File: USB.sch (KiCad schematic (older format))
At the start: 49 parts

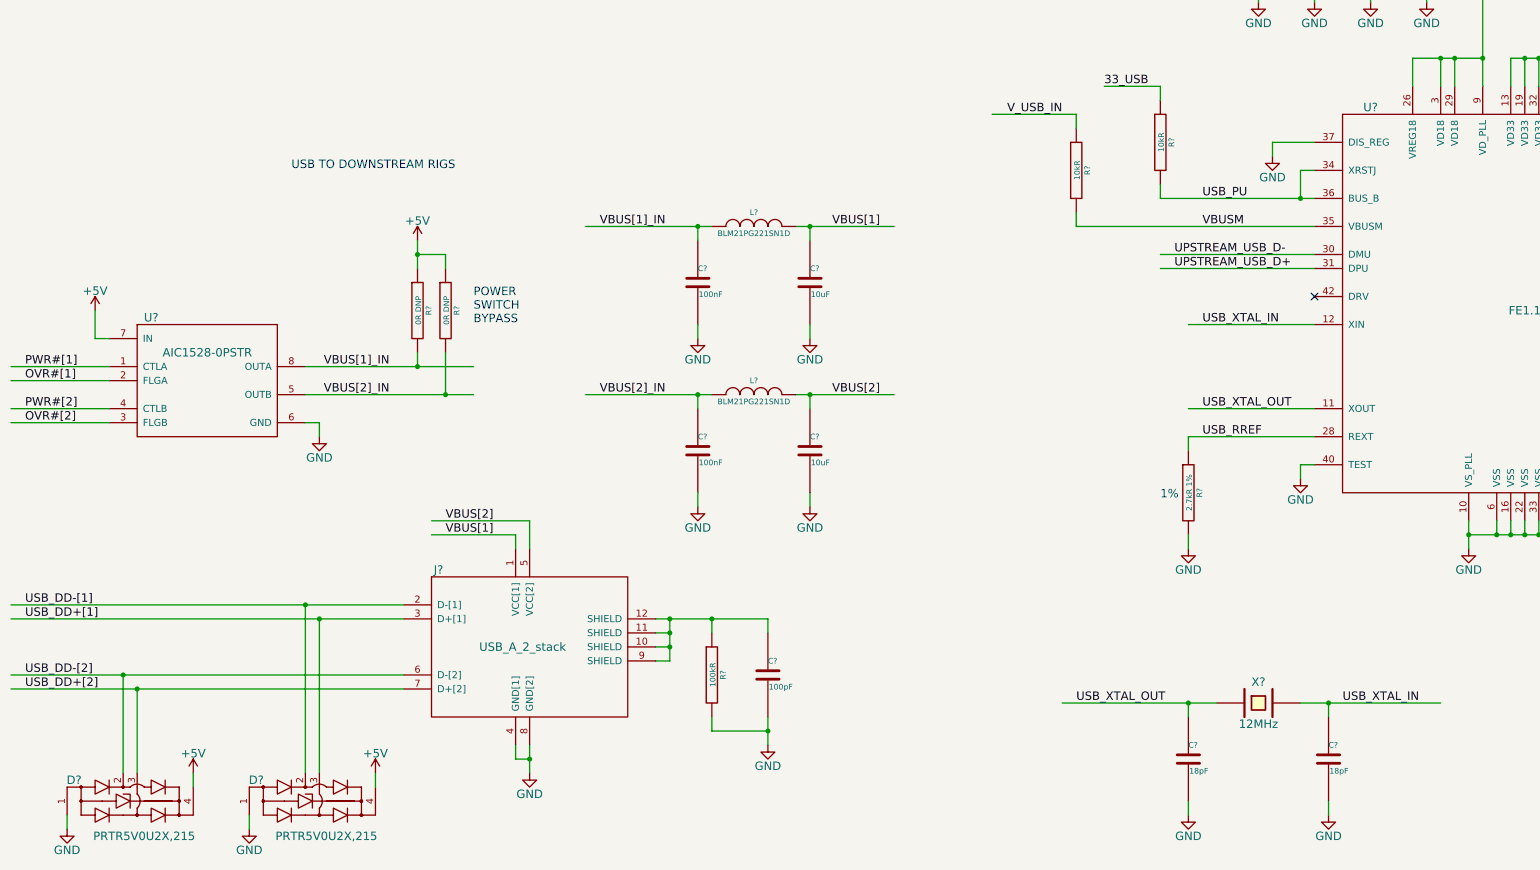
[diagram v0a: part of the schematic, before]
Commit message: added testpoint part number, small net naming changes
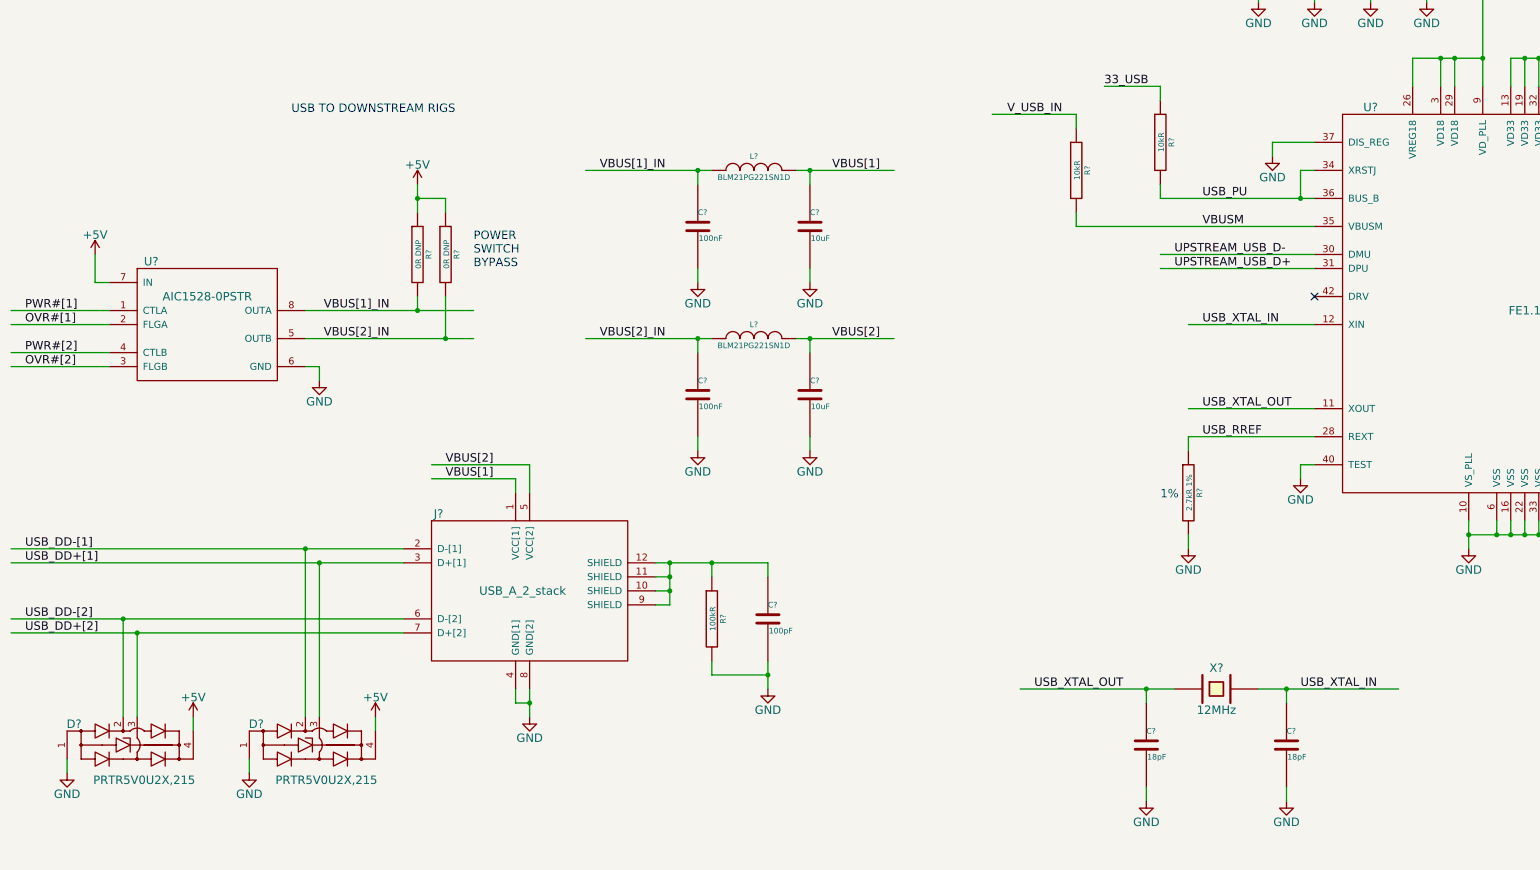
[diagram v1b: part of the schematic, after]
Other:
- moved on the sheet: C?, D?, J?, L?, R?, U?, X?

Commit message: annotated
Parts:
- gave numbers to parts that had none: 49

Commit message: annotated, netlist
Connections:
- wire segments 261 -> 199

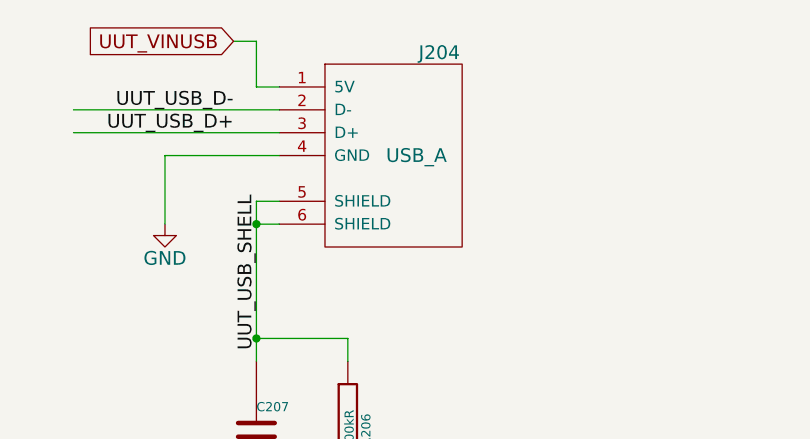
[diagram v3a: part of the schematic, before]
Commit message: swapped out new USB_A_TH symbol
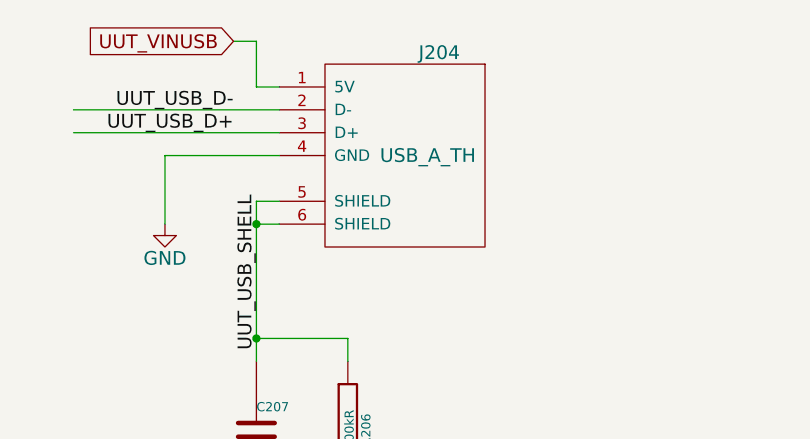
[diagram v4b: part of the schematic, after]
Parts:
- removed J204: USB_A, symbol USB_A
- added J204: USB_A_TH, symbol USB_A_TH
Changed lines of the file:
@@
 EESchema Schematic File Version 2
+LIBS:t2-hw-test-rig-rescue
 LIBS:power
 LIBS:device
@@
 LIBS:memory
 LIBS:xilinx
-LIBS:special
 LIBS:microcontrollers
 LIBS:dsp
@@
 	3650 3100 3650 3200
 $Comp
-L USB_A J204
-U 1 1 55427432
-P 9000 2000
-F 0 "J204" H 8900 2450 60  0000 C CNN
-F 1 "USB_A" H 9000 2000 60  0000 C CNN
-F 2 "" H 9600 2500 60  0000 C CNN
-F 3 "" H 9600 2500 60  0000 C CNN
-	1    9000 2000
-	-1   0    0    -1
-$EndComp
-$Comp
 L GND #PWR054
 U 1 1 554278A0
@@
 Wire Wire Line
 	8300 1500 8200 1500
+$Comp
+L USB_A_TH J204
+U 1 1 5547C2A7
+P 9000 2000
+F 0 "J204" H 8900 2450 60  0000 C CNN
+F 1 "USB_A_TH" H 8950 2000 60  0000 C CNN
+F 2 "" H 9600 2500 60  0000 C CNN
+F 3 "" H 9600 2500 60  0000 C CNN
+	1    9000 2000
+	-1   0    0    -1
+$EndComp
 $EndSCHEMATC

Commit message: unconventional library hack:moved tm lib above all others so parts come from there first
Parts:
- J204: footprint (none) -> tm-kicad-lib:USB-A
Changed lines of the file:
@@
 EESchema Schematic File Version 2
-LIBS:t2-hw-test-rig-rescue
+LIBS:tm-kicad-lib
 LIBS:power
 LIBS:device
@@
 LIBS:contrib
 LIBS:valves
-LIBS:tm-kicad-lib
 LIBS:t2-hw-test-rig-cache
 EELAYER 25 0
@@
 F 0 "J204" H 8900 2450 60  0000 C CNN
 F 1 "USB_A_TH" H 8950 2000 60  0000 C CNN
-F 2 "" H 9600 2500 60  0000 C CNN
+F 2 "tm-kicad-lib:USB-A" H 9600 2500 60  0001 C CNN
 F 3 "" H 9600 2500 60  0000 C CNN
 	1    9000 2000

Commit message: components and footprints
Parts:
- C222, C223: footprint tm-kicad-lib:SMD-0402-C -> tm-kicad-lib:SMD-0402
- J202: footprint (none) -> Pin_Headers:Pin_Header_Straight_1x02
- R203, R204: footprint tm-kicad-lib:SMD-0603-R -> tm-kicad-lib:SMD-0603
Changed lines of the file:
@@
 F 0 "R203" V 4280 6000 40  0000 C CNN
 F 1 "0R DNP" V 4207 6001 40  0000 C CNN
-F 2 "tm-kicad-lib:SMD-0603-R" V 4130 6000 30  0001 C CNN
+F 2 "tm-kicad-lib:SMD-0603" V 4130 6000 30  0001 C CNN
 F 3 "" H 4200 6000 30  0000 C CNN
 	1    4200 6000
@@
 	2200 3100 2200 3000
 Wire Wire Line
-	1800 3000 2200 3000
+	2200 3000 1800 3000
 Wire Wire Line
 	1800 2200 1800 3100
@@
 F 0 "R204" V 4480 6000 40  0000 C CNN
 F 1 "0R DNP" V 4407 6001 40  0000 C CNN
-F 2 "tm-kicad-lib:SMD-0603-R" V 4330 6000 30  0001 C CNN
+F 2 "tm-kicad-lib:SMD-0603" V 4330 6000 30  0001 C CNN
 F 3 "" H 4400 6000 30  0000 C CNN
 	1    4400 6000
@@
 F 0 "C223" H 16100 7500 40  0000 L CNN
 F 1 "1uF DNP" H 16106 7315 40  0000 L CNN
-F 2 "tm-kicad-lib:SMD-0402-C" H 16138 7250 30  0001 C CNN
+F 2 "tm-kicad-lib:SMD-0402" H 16138 7250 30  0001 C CNN
 F 3 "" H 16100 7400 60  0000 C CNN
 	1    16100 7400
@@
 F 0 "C222" H 15700 7500 40  0000 L CNN
 F 1 "1uF DNP" H 15706 7315 40  0000 L CNN
-F 2 "tm-kicad-lib:SMD-0402-C" H 15738 7250 30  0001 C CNN
+F 2 "tm-kicad-lib:SMD-0402" H 15738 7250 30  0001 C CNN
 F 3 "" H 15700 7400 60  0000 C CNN
 	1    15700 7400
@@
 F 0 "J202" H 4850 2050 50  0000 C CNN
 F 1 "CONN_01X02" V 4950 1900 50  0000 C CNN
-F 2 "" H 4850 1900 60  0000 C CNN
+F 2 "Pin_Headers:Pin_Header_Straight_1x02" H 4850 1900 60  0001 C CNN
 F 3 "" H 4850 1900 60  0000 C CNN
 	1    4850 1900
@@
 F 0 "JP201" H 4700 1750 50  0000 C CNN
 F 1 "JUMPER" H 4700 1520 50  0000 C CNN
-F 2 "" H 4700 1600 60  0000 C CNN
+F 2 "" H 4700 1600 60  0001 C CNN
 F 3 "" H 4700 1600 60  0000 C CNN
 	1    4700 1600
@@
 	8700 2900 8700 2800
 Wire Wire Line
-	8300 2800 8700 2800
+	8700 2800 8300 2800
 Wire Wire Line
 	8300 2200 8300 2900

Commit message: usb refactor on sch and pcb, mechanical constraints on bcp
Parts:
- removed C203, C209, C211, C212, C214, C215, C217: 100nF, tm-kicad-lib:SMD-0402-C, symbol TM_C
- removed C204: 100pF, tm-kicad-lib:SMD-0402-C, symbol TM_C
- removed C205, C206, C213, C216, C218, C219: 10uF, tm-kicad-lib:SMD-0805-C, symbol TM_C
- removed C208, C210: 18pF, tm-kicad-lib:SMD-0402-C, symbol TM_C
- removed C220, C221: 1uF, tm-kicad-lib:SMD-0402-C, symbol TM_C
- removed C222, C223: 1uF DNP, tm-kicad-lib:SMD-0402, symbol TM_C
- removed D202: PRTR5V0U2X,215, tm-kicad-lib:PRTR5V0U2X,215, symbol PRTR5V0U2X,215
- removed J203: USB_A_2_stack, tm-kicad-lib:Molex-0672983090, symbol USB_A_2_stack
- removed L201, L202: BLM21PG221SN1D, tm-kicad-lib:SMD-0805-R, symbol TM_L
- removed R204: 0R DNP, tm-kicad-lib:SMD-0603, symbol TM_R
- removed R205: 100kR, tm-kicad-lib:SMD-0402-R, symbol TM_R
- removed R207, R208: 10kR, tm-kicad-lib:SMD-0402-R, symbol TM_R
- removed R209: 2.7kR 1%, tm-kicad-lib:SMD-0402-R, symbol TM_R
- removed R210, R211, R212, R213: 1MR, tm-kicad-lib:SMD-0402-R, symbol TM_R
- removed U201: AIC1528-0PSTR, tm-kicad-lib:SOP-8, symbol AIC1528-0PSTR
- removed U202: FE1.1, tm-kicad-lib:CY7C65634-48AXCT, symbol FE1.1
- removed X201: 12MHz, tm-kicad-lib:Seeed-xtal-12MHz, symbol CRYSTAL
- added J203: MICROUSB-TH, tm-kicad-lib:Seeed-USB-Micro-320010028, symbol MICROUSB-TH
- C202: value 100nF -> 100pF
- R203: value 0R DNP -> 100kR; footprint tm-kicad-lib:SMD-0603 -> tm-kicad-lib:SMD-0402-R
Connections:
- net labels added: UUT_USB_PASSTHROUGH_SHELL
- net labels removed: 33_USB, OVR#[1], OVR#[2], PWR#[1], PWR#[2], UPSTREAM_USB_D+, UPSTREAM_USB_D-, USB_18, USB_DD+[1], USB_DD+[2], USB_DD-[1], USB_DD-[2], USB_PU, USB_RREF, USB_XTAL_IN, USB_XTAL_OUT, VBUSM, VBUS[1], VBUS[1]_IN, VBUS[2], VBUS[2]_IN
- wire segments 199 -> 62
- no-connect marks 8 -> 3
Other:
- note added: "SAM USB"
- note added: "UUT USB PASSTHROUGH\nWITH POWER SPLICE"
- note removed: "1%"
- note removed: "POWER\nSWITCH\nBYPASS"
- note removed: "USB TO DOWNSTREAM RIGS"
- moved on the sheet: C201, C207, D203, J201, J202, J204, JP201, R201, R202, R206
